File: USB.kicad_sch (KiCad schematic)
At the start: 9 parts, among them P2101 USB-C

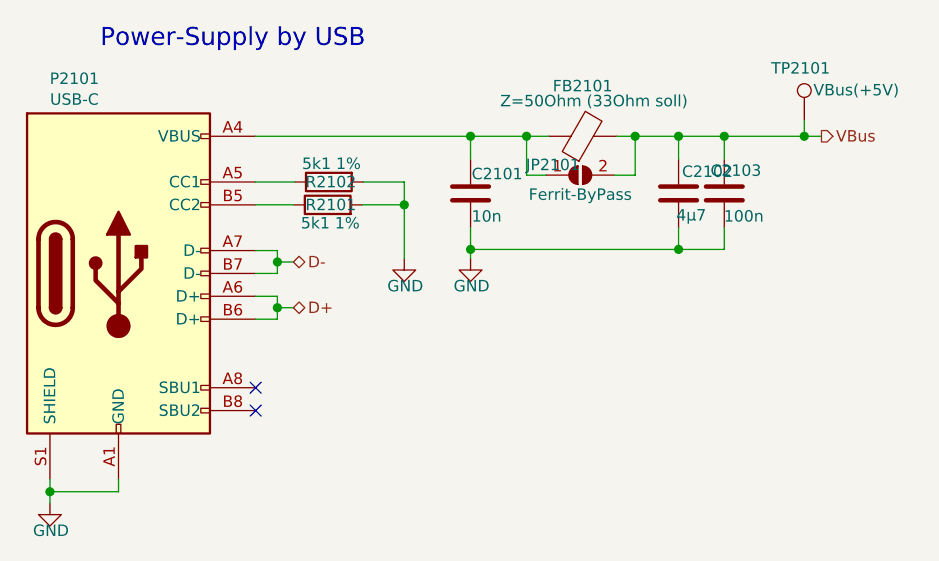
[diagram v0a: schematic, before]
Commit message: FEAR-16 V2.2
PCB-Changes:
 - Added rudimentary "load-balancer" (not really a balancer, but should avoid the DC/DC from regulating against each other!)
 - Added optional GND-jumpers to the N/C pins of the shields
 - Modified amplification adjustment:
   -> Added a offset resistor in row to the trim-poti for amplification for finer amp-tuning
   -> Reduced trim-poti-value from 1Meg -> 50k (20x finer adjustment-range)
      Poti can in the range of:
      - 30k (min) for being able to reach the correct amplification
      - 50k (max) for having at least 20x finer tune-range and a bit of reserve, as 30k is pretty thight on tolerance

Misc.:
 - Added LICENSE.md
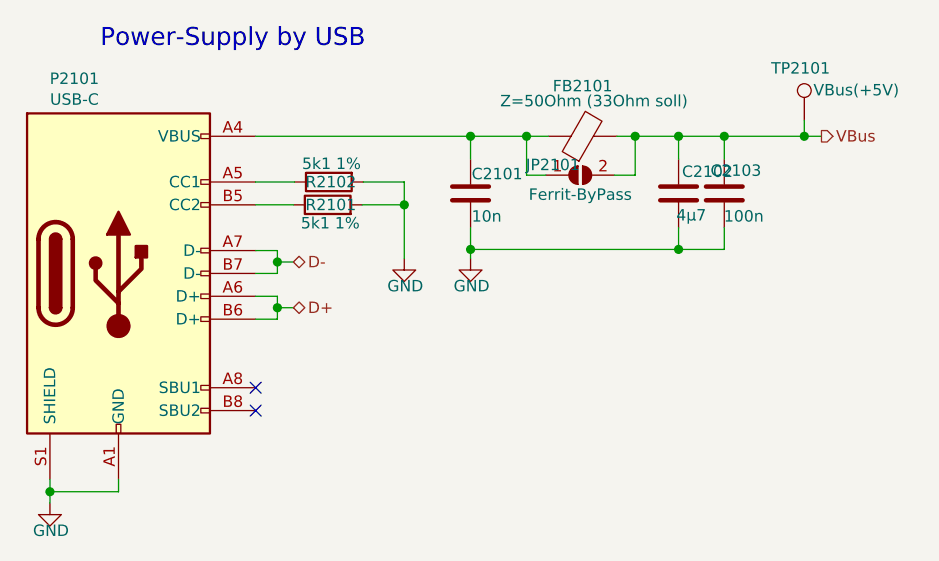
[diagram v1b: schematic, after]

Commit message: Finished README.md
- Adjustment in .gitignore
- Finished first README.md attempt
- Added extra comments to "5V_Supplies"
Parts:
- FB2101: value Z=50Ohm (33Ohm soll) -> Z=50Ω (33Ω soll) (opt.)
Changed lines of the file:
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@@
 			)
 		)
-		(property "Value" "Z=50Ohm (33Ohm soll)"
+		(property "Value" "Z=50Ω (33Ω soll) (opt.)"
 			(at 84.582 25.419 90)
 			(effects
